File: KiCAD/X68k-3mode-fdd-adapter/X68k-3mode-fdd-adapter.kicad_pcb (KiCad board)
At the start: 2 copper layers, 53 x 72 mm, 50 parts, among them J1 Conn_02x17_Odd_Even, J2 Conn_02x17_Odd_Even, J3 Conn_01x04, J4 Conn_01x04, J5 Conn_01x02_Pin, J6 Conn_01x04, J7 Conn_01x05_Pin, J8 Conn_01x05_Pin, Q1 2SC4213, SW1 SW_DIP_x04, U1 CH32V003F4U6, U2 74HC14, U3 74HC14, U4 74HC153, U5 74HC153, U6 ULN2003A

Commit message: 一通り配線した(未チェック)
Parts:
- removed J7, J8: Conn_01x05_Pin, Connector_PinHeader_1.27mm:PinHeader_1x05_P1.27mm_Vertical
- removed R11: 1K, Resistor_SMD:R_0603_1608Metric
- removed U2, U3: 74HC14, Package_SO:SO-14_5.3x10.2mm_P1.27mm
- added SW2: SW_SPDT, Connector_PinHeader_2.54mm:PinHeader_1x03_P2.54mm_Vertical, F.Cu at (80.5, 106.7)
- added TP6: TestPoint, TestPoint:TestPoint_Pad_1.0x1.0mm, B.Cu at (108.0, 107.4)
- BZ1: footprint Buzzer_Beeper:Buzzer_12x9.5RM7.6 -> x68k-lib:UGCT7525AN4
- D3: moved to F.Cu
- J1: footprint Connector_IDC:IDC-Header_2x17_P2.54mm_Vertical -> x68k-lib:PinHeader_2x17_P2.54mm_Horizontal_Mirror
- J2: footprint Connector_IDC:IDC-Header_2x17_P2.54mm_Vertical -> x68k-lib:PinSocket_2x17_P2.54mm_Horizontal_Mirror
- J6: footprint Connector_PinHeader_2.54mm:PinHeader_1x04_P2.54mm_Vertical -> Connector_PinSocket_2.54mm:PinSocket_1x04_P2.54mm_Vertical
- JP1, JP2, R1, R10, R12, R2, R3, R4, R5, R6, R7, R8, R9, TP1, TP2, TP4, TP5: moved to B.Cu
- moved R20 89.4 mm to (94.4, 101.0)
- moved R17 86.2 mm to (94.4, 108.0)
- moved R21 85.5 mm to (94.4, 97.8)
- moved R8 83.6 mm to (78.5, 81.3), turned to 180 degrees
- moved R18 83.1 mm to (94.4, 106.0)
- moved R9 79.8 mm to (78.5, 75.9), turned to 180 degrees
- moved R12 78.1 mm to (78.5, 79.5), turned to 180 degrees
- moved R14 77.6 mm to (80.5, 62.7), turned to 180 degrees
- moved R10 77.3 mm to (78.5, 72.4), turned to 180 degrees
- moved R15 77.3 mm to (80.5, 64.3), turned to 180 degrees
- moved R16 77.0 mm to (80.5, 65.8), turned to 180 degrees
- moved R4 72.9 mm to (78.5, 70.6), turned to 180 degrees
- moved R6 72.4 mm to (78.5, 74.2), turned to 180 degrees
- moved R3 72.2 mm to (78.5, 66.0), turned to 180 degrees
- moved R2 72.2 mm to (78.5, 63.5), turned to 180 degrees
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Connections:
- net /OPTION_SELECT_MAIN renamed /OPTION_SELECT
- net /OPTION_SELECT_SUB renamed /OPTION_SELECT_PAIR
- J2 pad 34: /READY -> /DISK_CHANGE
- U1 pad 18: /EJECT_MASK_BUF -> /EJECT_MASK
- U1 pad 19: /EJECT_BUF -> /EJECT
- U1 pad 20: /LED_BLINK_BUF -> /LED_BLINK
- U4 pad 10: /OPTION_SELECT_1_BUF -> /OPTION_SELECT_1
- U4 pad 11: /OPTION_SELECT_2_BUF -> /OPTION_SELECT_2
- U4 pad 12: /OPTION_SELECT_3_BUF -> /OPTION_SELECT_3
- U4 pad 13: /OPTION_SELECT_0_BUF -> /OPTION_SELECT_0
- U4 pad 3: /OPTION_SELECT_3_BUF -> /OPTION_SELECT_3
- U4 pad 4: /OPTION_SELECT_2_BUF -> /OPTION_SELECT_2
- U4 pad 5: /OPTION_SELECT_1_BUF -> /OPTION_SELECT_1
- U4 pad 6: /OPTION_SELECT_0_BUF -> /OPTION_SELECT_0
- U5 pad 3: /DRIVE_SELECT_3_BUF -> /DRIVE_SELECT_3
- U5 pad 4: /DRIVE_SELECT_2_BUF -> /DRIVE_SELECT_2
- U5 pad 5: /DRIVE_SELECT_1_BUF -> /DRIVE_SELECT_1
- U5 pad 6: /DRIVE_SELECT_0_BUF -> /DRIVE_SELECT_0
- U6 pad 10: Net-(J8-Pin_5) -> unconnected-(U6-O7-Pad10)
- U6 pad 11: Net-(J8-Pin_4) -> unconnected-(U6-O6-Pad11)
- U6 pad 12: Net-(J8-Pin_3) -> unconnected-(U6-O5-Pad12)
- U6 pad 13: Net-(J8-Pin_2) -> unconnected-(U6-O4-Pad13)
- U6 pad 14: Net-(J8-Pin_1) -> unconnected-(U6-O3-Pad14)
- U6 pad 16: /READY -> /READY_GEN_BUF
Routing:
- net GND: track 0.00 -> 122.1 mm, vias 0 -> 44
- net /OPTION_SELECT_0: track 0.00 -> 57.7 mm, vias 0 -> 6
- net /OPTION_SELECT_1: track 0.00 -> 56.1 mm, vias 0 -> 5
- net /DIPSW_0: track 0.00 -> 56.0 mm, vias 0 -> 4
- net /OPTION_SELECT_2: track 0.00 -> 52.6 mm, vias 0 -> 4
- net /OPTION_SELECT_3: track 0.00 -> 47.7 mm, vias 0 -> 3
- net /INDEX: track 0.00 -> 46.2 mm, vias 0 -> 3
- net +5V: track 0.00 -> 43.4 mm, vias 0 -> 18
- net /DIPSW_1: track 0.00 -> 39.7 mm, vias 0 -> 3
- net /MOTOR_ON: track 0.00 -> 37.4 mm, vias 0 -> 1
- net /READY_GEN: track 0.00 -> 37.0 mm, vias 0 -> 2
- net /TRACK_00: track 0.00 -> 34.7 mm
- net /DISK_IN: track 0.00 -> 34.6 mm
- net /SIDE_SELECT: track 0.00 -> 34.1 mm
- net /WRITE_PROTECT: track 0.00 -> 33.0 mm
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- added copper zone on In1.Cu, net +5V
- added copper zone on B.Cu, net GND
- added copper zone on F.Cu, net GND
- added copper zone on In2.Cu, net GND
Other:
- board size 53 x 72 mm -> 45 x 70 mm
- copper layers 2 -> 4

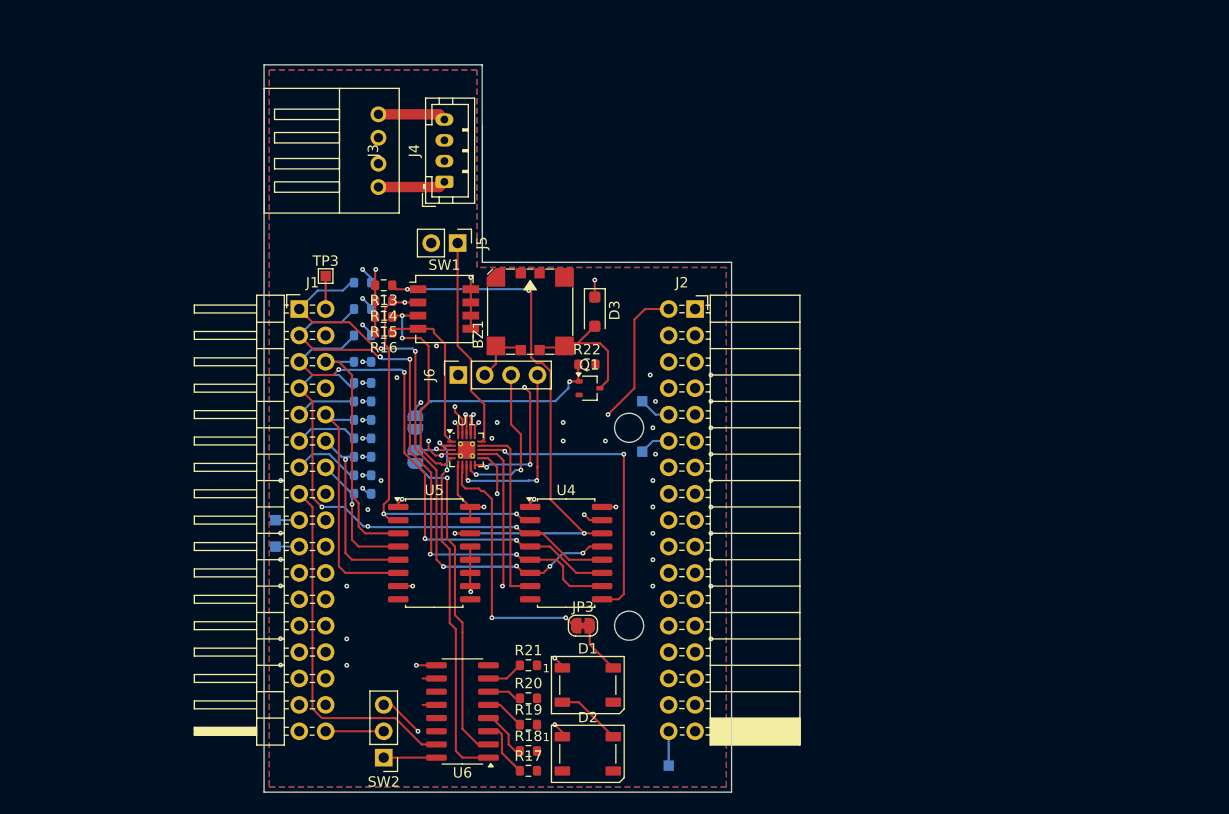
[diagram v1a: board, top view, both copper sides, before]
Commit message: 一通りの配線、調整を入れたバージョン
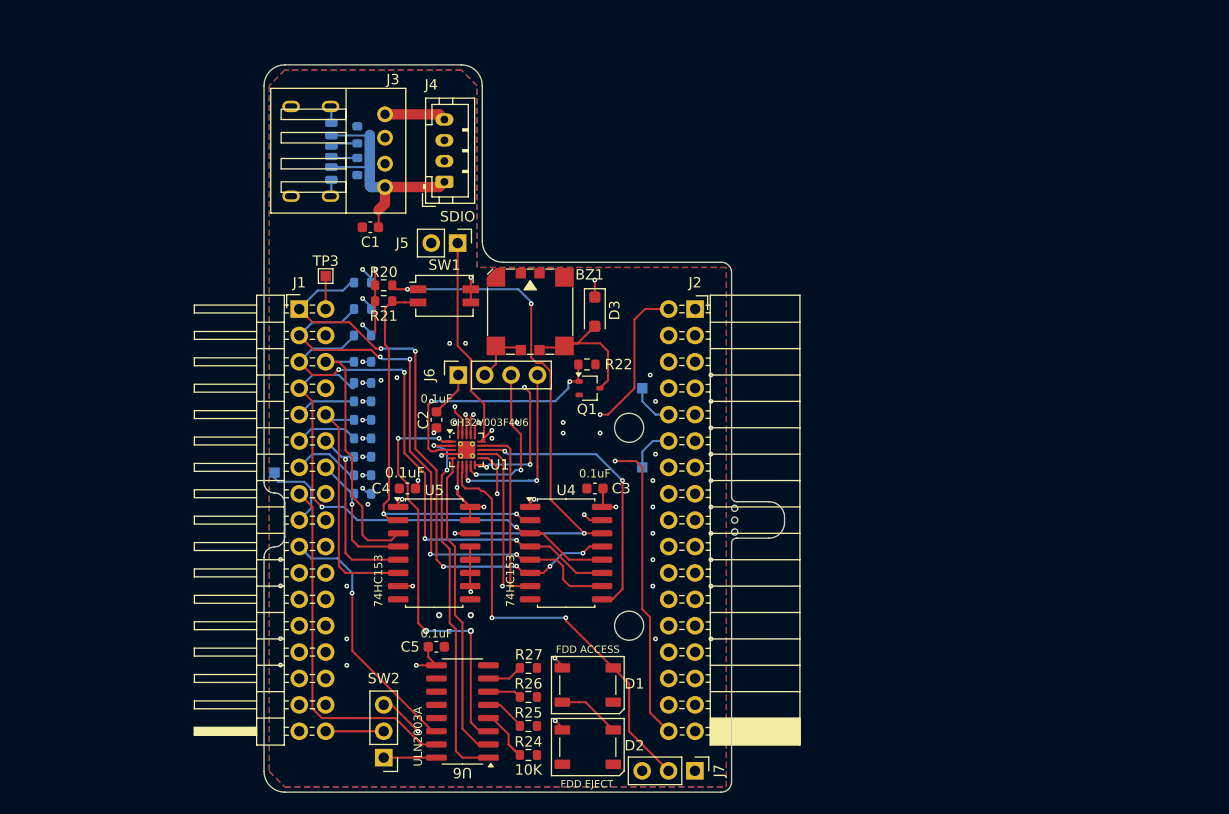
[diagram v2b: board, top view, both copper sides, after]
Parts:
- removed JP1, JP2: Jumper_2_Small_Open, Jumper:SolderJumper-2_P1.3mm_Open_RoundedPad1.0x1.5mm
- removed JP3: Jumper_2_Bridged, Jumper:SolderJumper-2_P1.3mm_Bridged_RoundedPad1.0x1.5mm
- removed R15, R16: 10K, Resistor_SMD:R_0603_1608Metric
- removed R17: 0, Resistor_SMD:R_0603_1608Metric
- removed TP5, TP6: TestPoint, TestPoint:TestPoint_Pad_1.0x1.0mm
- added C1: 10uF, Capacitor_SMD:C_0603_1608Metric, F.Cu at (79.2, 55.6)
- added C2: 0.1uF, Capacitor_SMD:C_0603_1608Metric, F.Cu at (85.6, 74.2)
- added C3: 0.1uF, Capacitor_SMD:C_0603_1608Metric, F.Cu at (100.9, 80.8)
- added C4: 0.1uF, Capacitor_SMD:C_0603_1608Metric, F.Cu at (82.8, 80.8)
- added C5: 0.1uF, Capacitor_SMD:C_0603_1608Metric, F.Cu at (85.6, 96.0)
- added J7: Conn_01x03_Pin, Connector_PinHeader_2.54mm:PinHeader_1x03_P2.54mm_Vertical, F.Cu at (110.5, 108.0)
- added P1: USB_C_Plug_USB2.0, Connector_USB:USB_C_Receptacle_GCT_USB4125-xx-x-0190_6P_TopMnt_Horizontal, B.Cu at (72.4, 48.3)
- added R31: 5.1k, Resistor_SMD:R_0603_1608Metric, B.Cu at (78.0, 49.8)
- added R32: 5.1k, Resistor_SMD:R_0603_1608Metric, B.Cu at (78.0, 46.7)
- D1: value WS2812B -> FDD ACCESS
- D2: value WS2812B -> FDD EJECT
- J5: value Conn_01x02_Pin -> SDIO
- R24: renamed from R18; value 0 -> 10K
- R25: renamed from R19; value 0 -> 10K
- R26: renamed from R20; value 0 -> 10K
- R27: renamed from R21; value 0 -> 10K
- SW1: value SW_DIP_x04 -> SW_DIP_x02; footprint Button_Switch_SMD:SW_DIP_SPSTx04_Slide_Copal_CHS-04A_W5.08mm_P1.27mm_JPin -> Button_Switch_SMD:SW_DIP_SPSTx02_Slide_Copal_CHS-02A_W5.08mm_P1.27mm_JPin
- moved TP4 4.57 mm to (70.0, 79.2)
- moved TP2 1.52 mm to (105.4, 78.7)
- moved SW1 1.27 mm to (86.4, 62.2)
- moved TP1 1.27 mm to (105.4, 71.1)
- moved D2 0.65 mm to (100.2, 105.7)
- moved J3 0.63 mm to (80.6, 48.3)
- moved R24 0.38 mm to (94.4, 106.4)
- moved R27 0.25 mm to (94.4, 98.0)
- moved R25 0.13 mm to (94.4, 103.6)
- moved R26 0.13 mm to (94.4, 100.8)
- renumbered R1 to R0, R2 to R1, R6 to R10, R7 to R11, R8 to R12, R5 to R13, R3 to R2, R13 to R20, R14 to R21, R4 to R3, R10 to R5, R9 to R6, R12 to R7
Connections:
- D1 pad 4: Net-(D1-DIN) -> /LED_DATA
- J1 pad 19: /FDD_INT -> /FDD_INT_BUF
- J2 pad 34: /DISK_CHANGE -> /DISK_CHANGE_DOSV
- J5 pad 1: Net-(J5-Pin_1) -> /DISK_CHANGE_DOSV
- SW1 pad 3: /DIPSW_2 -> +5V
- SW1 pad 4: /DIPSW_3 -> +5V
- SW2 pad 3: /DISK_CHANGE -> /DISK_CHANGE_DOSV
- U1 pad 1: /DIPSW_3 -> /FDD_INT_GEN
- U1 pad 15: Net-(J5-Pin_1) -> /DISK_CHANGE_DOSV
- U1 pad 3: Net-(JP1-B) -> /BUZZER
- U1 pad 5: /DIPSW_2 -> /DISK_IN_GEN
- U6 pad 14: unconnected-(U6-O3-Pad14) -> /FDD_INT_BUF
- U6 pad 3: Net-(U6-I3) -> /FDD_INT_GEN
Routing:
- net /DISK_CHANGE_DOSV: track 0.00 -> 92.7 mm, vias 0 -> 3
- net /FDD_INT_GEN: track 0.00 -> 40.8 mm, vias 0 -> 4
- net /DISK_CHANGE: track 31.8 -> 0.00 mm, vias 1 -> 0
- net +5V: track 43.4 -> 69.7 mm, vias 18 -> 21
- net /FDD_INT_BUF: track 0.00 -> 25.0 mm, vias 0 -> 1
- net /DIPSW_2: track 21.7 -> 0.00 mm, vias 2 -> 0
- net Net-(J5-Pin_1): track 20.3 -> 0.00 mm
- net /LED_DATA: track 25.2 -> 42.8 mm
- net /DIPSW_3: track 15.6 -> 0.00 mm
- net GND: track 122.1 -> 130.8 mm
- net /ERR_DISK: track 2.29 -> 7.97 mm
- net Net-(U6-I3): track 5.65 -> 0.00 mm
- net Net-(JP1-B): track 5.56 -> 0.00 mm, vias 1 -> 0
- net Net-(D1-DIN): track 5.28 -> 0.00 mm
- net /BUZZER: track 20.6 -> 24.0 mm
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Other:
- board size 45 x 70 mm -> 50.1 x 70 mm
- board text added: "DISK T SEL NC DRIVE SEL 3 INDEX DRIVE SEL 0 DRIVE SEL 1 DRIVE SEL 2 MOTOR ON DIRECTION STEP WRITE DATA WRITE GATE TRACK00 W PROTECT READ DATA SIDE SEL READY"
- board text added: "DSEL0"
- board text added: "DSEL1"
- board text added: "Developed by @kunichiko and @kani7. January 2025 (V1.0.0)"
- board text added: "EDSK"
- board text added: "MODE SEL NC NC INDEX DRIVE SEL 0 DRIVE SEL 1 NC MOTOR ON DIRECTION STEP WRITE DATA WRITE GATE TRACK00 W PROTECT READ DATA SIDE SEL DISK CHG"
- board text added: "Minyas X"
- board text added: "NC KEY GND GND GND GND GND GND GND GND GND GND GND GND GND GND GND"
- board text added: "OPT 0 OPT 1 OPT 2 OPT 3 EJECT EJECT MASK LED BLINK DISK IN ERR DISK FDD INT GND GND GND GND GND GND GND"
- board text added: "PC FDD"
- board text added: "PC FDD Converter for X680x0 series"
- board text added: "X680x0"

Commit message: 基板形状を見直した
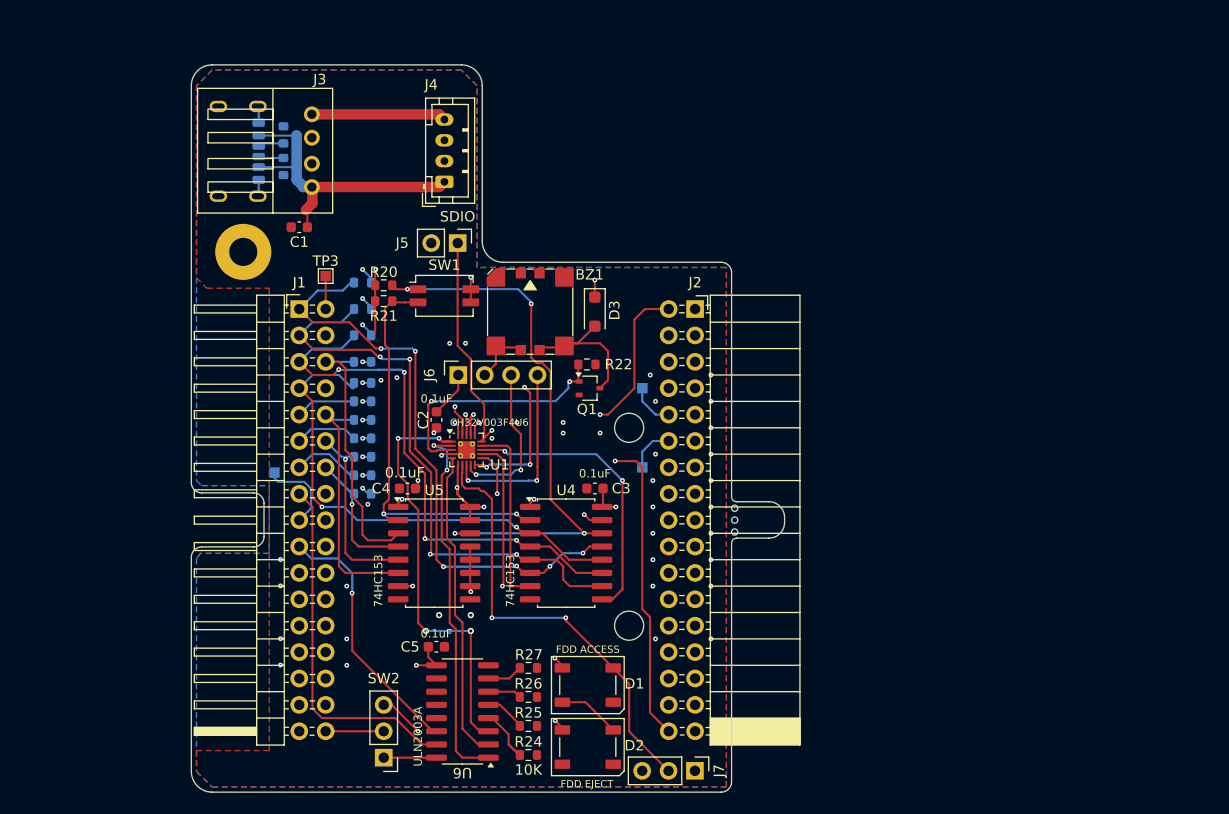
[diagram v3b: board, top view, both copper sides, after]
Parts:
- added H1: MountingHole_Pad, MountingHole:MountingHole_2.7mm_M2.5_Pad, F.Cu at (67.0, 58.0)
- moved R31 7.11 mm to (70.9, 49.8)
- moved R32 7.11 mm to (70.9, 46.7)
- moved J3 7.04 mm to (73.6, 48.3)
- moved P1 7.00 mm to (65.4, 48.3)
- moved C1 6.84 mm to (72.4, 55.6)
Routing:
- net +5V: track 69.7 -> 77.2 mm
- net +12V: track 5.92 -> 13.0 mm
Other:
- board size 50.1 x 70 mm -> 57.1 x 70 mm

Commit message: v1.0.0注文版
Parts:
- D1: value FDD ACCESS -> SK6812MINI; footprint LED_SMD:LED_WS2812B_PLCC4_5.0x5.0mm_P3.2mm -> x68k-lib:SK6812MINI-HS
- D2: value FDD EJECT -> SK6812MINI; footprint LED_SMD:LED_WS2812B_PLCC4_5.0x5.0mm_P3.2mm -> x68k-lib:SK6812MINI-HS
- D3: value D_Schottky -> SS2040FL
- J4: value Conn_01x04 -> PH-4A
- Q1: value 2SC4213 -> 2SC2712; footprint Package_TO_SOT_SMD:SOT-323_SC-70 -> Package_TO_SOT_SMD:SOT-23
- SW1: footprint Button_Switch_SMD:SW_DIP_SPSTx02_Slide_Copal_CHS-02A_W5.08mm_P1.27mm_JPin -> Button_Switch_SMD:SW_DIP_SPSTx02_Slide_Copal_CHS-02B_W7.62mm_P1.27mm
- moved R21 4.67 mm to (78.7, 58.4), turned to 90 degrees
- moved TP4 4.57 mm to (70.1, 83.8)
- moved R20 2.90 mm to (81.3, 58.4), turned to 90 degrees
- moved SW1 1.27 mm to (85.1, 62.2)
- moved D2 1.03 mm to (100.3, 104.6)
- moved D1 0.66 mm to (100.3, 99.1)
- moved Q1 0.36 mm to (100.6, 71.4)
- turned R22 to 180 degrees
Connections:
- D1 pad 1: +5V -> GND
- D1 pad 2: Net-(D1-DOUT) -> /LED_DATA
- D1 pad 3: GND -> +5V
- D1 pad 4: /LED_DATA -> Net-(D1-DOUT)
- D2 pad 1: +5V -> GND
- D2 pad 2: unconnected-(D2-DOUT-Pad2) -> Net-(D1-DOUT)
- D2 pad 3: GND -> +5V
- D2 pad 4: Net-(D1-DOUT) -> unconnected-(D2-DOUT-Pad4)
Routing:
- net /ERR_DISK: track 7.97 -> 2.29 mm
- net GND: track 130.8 -> 125.1 mm, vias 44 -> 46
- net +5V: track 77.2 -> 79.9 mm, vias 21 -> 20
- net /LED_DATA: track 42.8 -> 45.4 mm
- net /DIPSW_1: track 39.7 -> 42.2 mm
- net /DIPSW_0: track 54.4 -> 56.7 mm
- net /BUZZER: track 24.0 -> 25.8 mm
- net Net-(D1-DOUT): track 6.01 -> 5.28 mm
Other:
- board text added: "ACCESS"
- board text added: "EJECT"

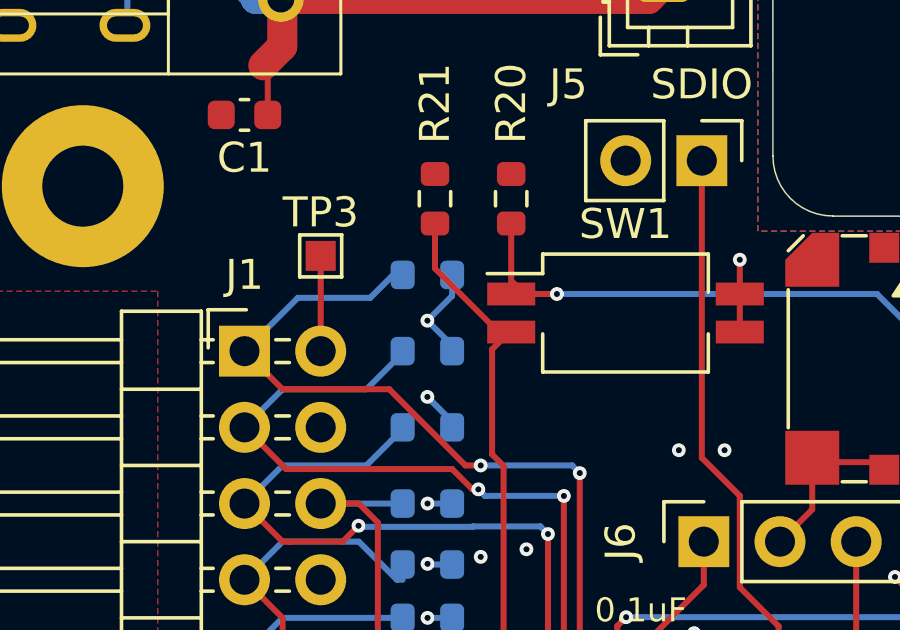
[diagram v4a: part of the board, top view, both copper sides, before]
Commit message: LCIC→LCSCに修正
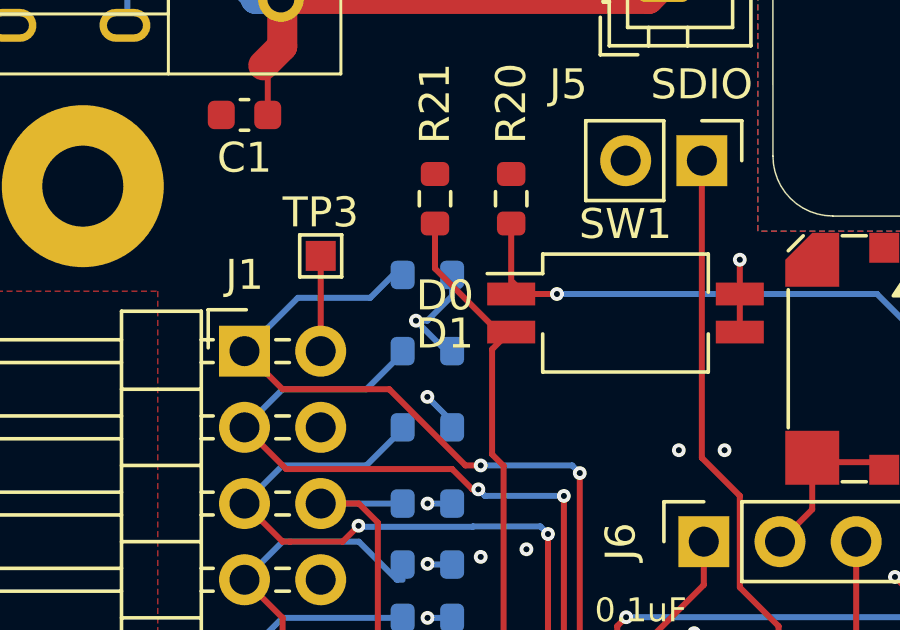
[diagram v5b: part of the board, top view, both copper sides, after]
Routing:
- net +5V: track 79.9 -> 80.8 mm
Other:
- board text added: "D0"
- board text added: "D1"
- board text added: "Developed by @kunichiko and @kani7. January 2025 (V1.0.1)"
- board text removed: "Developed by @kunichiko and @kani7. January 2025 (V1.0.0)"

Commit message: BuzzerシンボルをSpeakerシンボルに変更
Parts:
- BZ1: value Buzzer -> Speaker
- J2: value Conn_02x17_Odd_Even -> Double Row 3A Copper Alloy 34P Female Headers (PM254-2-17-W-8.5)

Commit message: 現状をコミット(特に修正はしていないはずだが……)
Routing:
- net GND: track 125.1 -> 133.5 mm, vias 46 -> 48
